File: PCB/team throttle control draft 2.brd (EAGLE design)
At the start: 75.9 x 59.7 mm, 15 parts, among them IC1 ICL7663CPA, IC4 7805T

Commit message: It was missing two connections so this is now fixed and fully operating design
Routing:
- net WH_SP3_D: track 0.00 -> 20.9 mm
- net WH_SP4_D: track 0.00 -> 20.9 mm
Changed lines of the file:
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@@
 <contactref element="WHEEL_SP3" pad="2"/>
 <contactref element="U$3" pad="18-A4/SDA0"/>
-<wire x1="53.34" y1="50.8" x2="53.34" y2="66.04" width="0" layer="19" extent="1-1"/>
+<wire x1="53.34" y1="66.04" x2="52.07" y2="64.77" width="0.3048" layer="16"/>
+<wire x1="52.07" y1="64.77" x2="49.53" y2="64.77" width="0.3048" layer="16"/>
+<wire x1="49.53" y1="64.77" x2="48.26" y2="63.5" width="0.3048" layer="16"/>
+<wire x1="48.26" y1="63.5" x2="48.26" y2="62.23" width="0.3048" layer="16"/>
+<wire x1="53.34" y1="57.15" x2="53.34" y2="50.8" width="0.3048" layer="16"/>
+<wire x1="48.26" y1="62.23" x2="53.34" y2="57.15" width="0.3048" layer="16"/>
 </signal>
 <signal name="WH_SP4_D">
 <contactref element="WHEEL_SP4" pad="2"/>
 <contactref element="U$3" pad="19-A5/SCL0"/>
-<wire x1="50.8" y1="50.8" x2="50.8" y2="66.04" width="0" layer="19" extent="1-1"/>
+<wire x1="45.72" y1="63.5" x2="45.72" y2="59.69" width="0.3048" layer="16"/>
+<wire x1="45.72" y1="59.69" x2="50.8" y2="54.61" width="0.3048" layer="16"/>
+<wire x1="50.8" y1="54.61" x2="50.8" y2="50.8" width="0.3048" layer="16"/>
+<wire x1="50.8" y1="66.04" x2="48.26" y2="66.04" width="0.3048" layer="16"/>
+<wire x1="48.26" y1="66.04" x2="45.72" y2="63.5" width="0.3048" layer="16"/>
 </signal>
 <signal name="ACC_DATA_OUT_1">

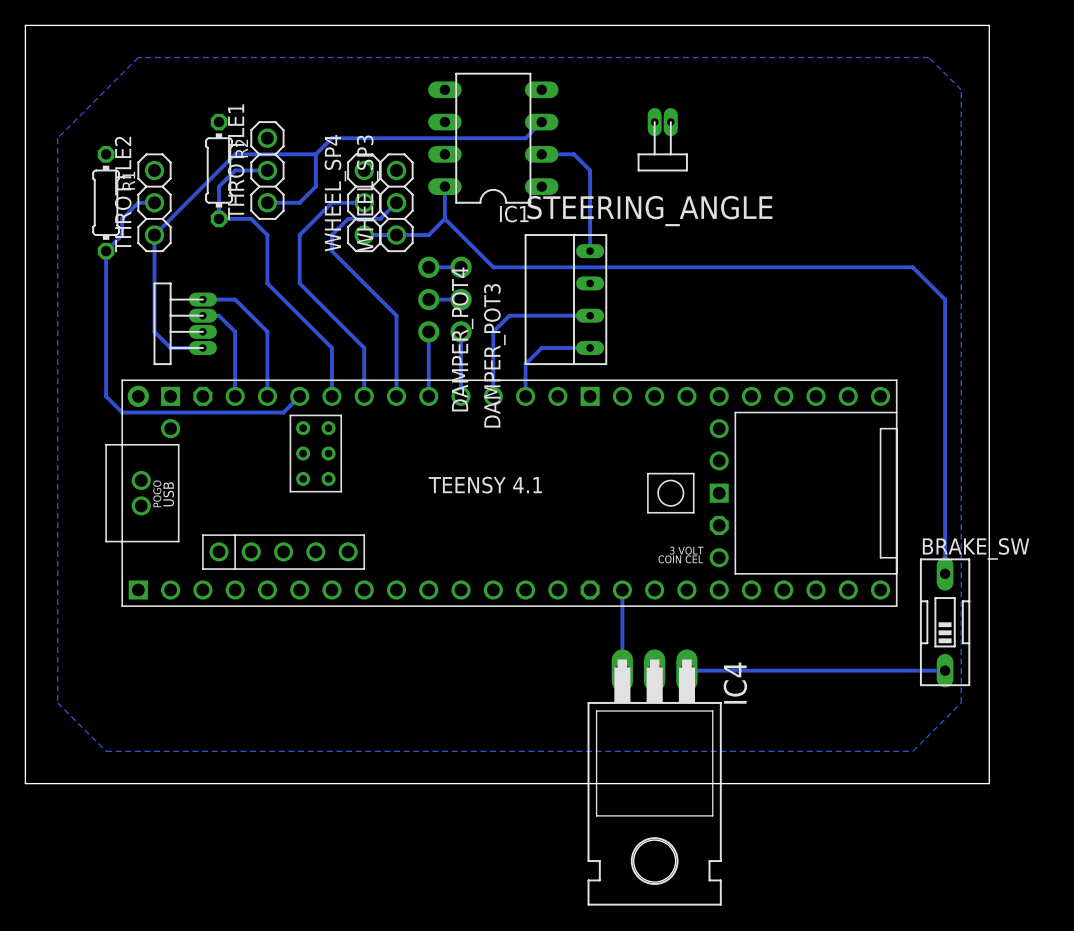
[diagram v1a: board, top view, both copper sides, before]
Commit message: Remove voltage regulator. Add 3-pin header. Connect 3.3V wire
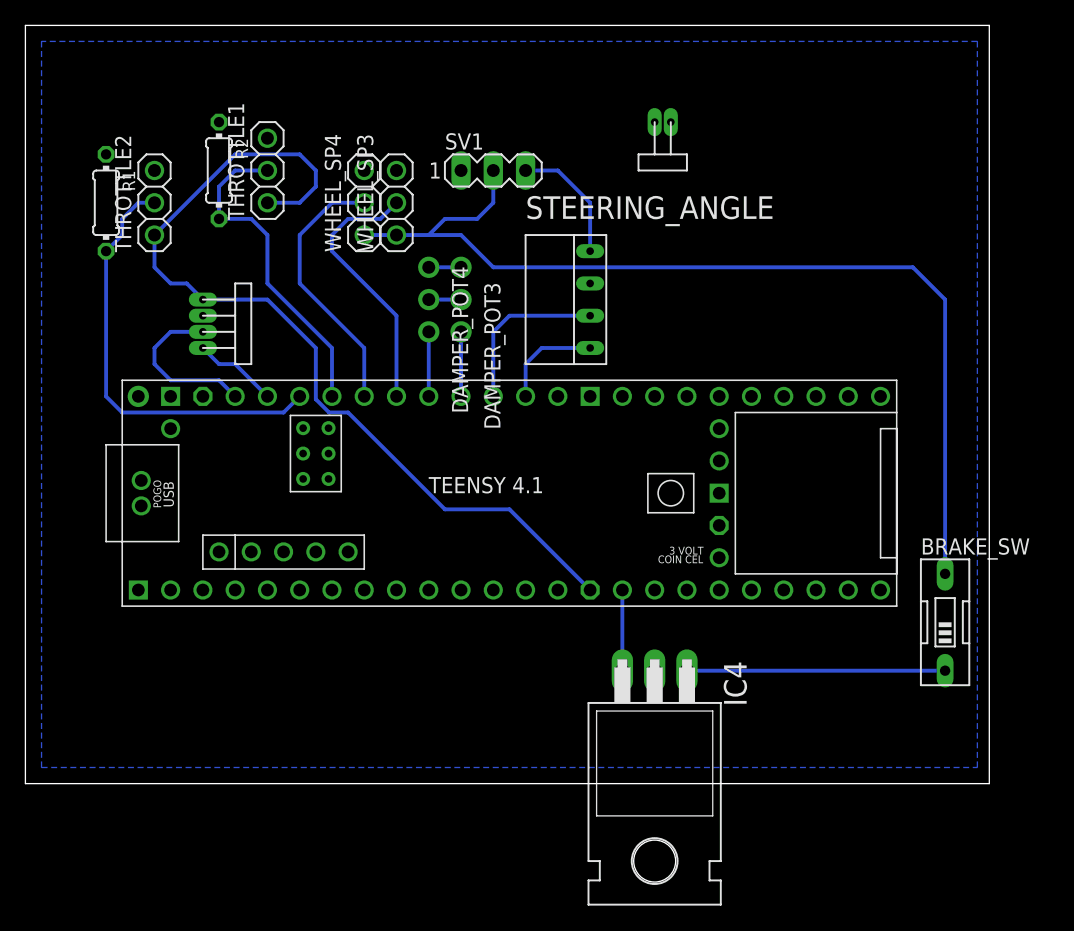
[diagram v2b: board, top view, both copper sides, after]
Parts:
- removed IC1: ICL7663CPA, maxim:DIL08
- added SV1: (no value), con-lstb:MA03-1
- moved U$11 9.25 mm to (36.8, 61.0), turned to 270 degrees
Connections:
- net 12V: now also SV1.2; no longer IC1.8
- net 3.3V: now also U$3.3V3-1; no longer IC1.3
- net 5V: now also SV1.3; no longer IC1.2
- net GND: now also SV1.1; no longer IC1.4
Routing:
- net 3.3V: track 53.0 -> 71.2 mm
- net 12V: track 73.0 -> 78.1 mm
- net CRX_2: track 8.15 -> 13.0 mm
- net CTX_2: track 11.2 -> 6.66 mm
- net 5V: track 10.7 -> 9.94 mm

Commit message: Retry polygon to fix GND signal
didn't work.
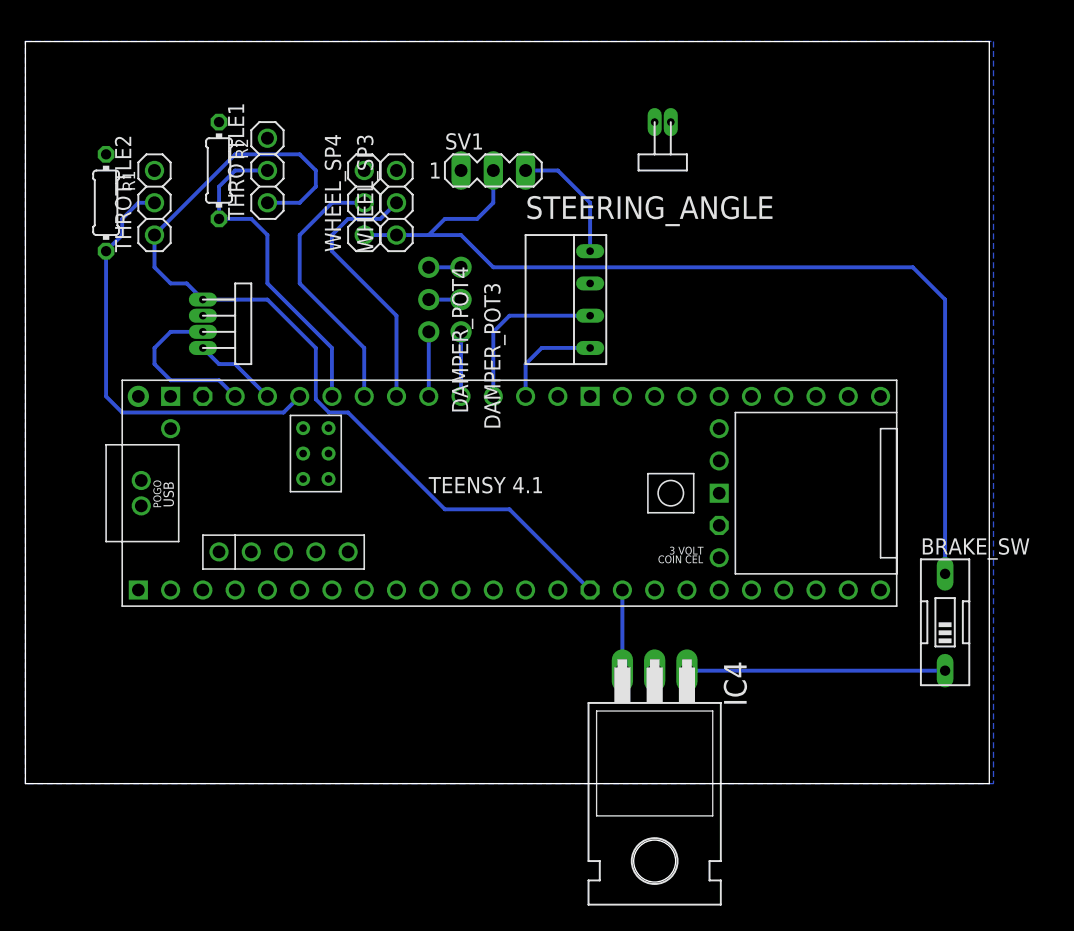
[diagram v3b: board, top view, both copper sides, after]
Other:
- board size 75.9 x 59.7 mm -> 75.9 x 58.4 mm
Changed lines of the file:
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@@
 <plain>
 <wire x1="24.13" y1="20.32" x2="100" y2="20.32" width="0" layer="20"/>
-<wire x1="100" y1="20.32" x2="100" y2="80" width="0" layer="20"/>
-<wire x1="100" y1="80" x2="24.13" y2="80" width="0" layer="20"/>
-<wire x1="24.13" y1="80" x2="24.13" y2="20.32" width="0" layer="20"/>
+<wire x1="100" y1="20.32" x2="100" y2="78.73" width="0" layer="20"/>
+<wire x1="100" y1="78.73" x2="24.13" y2="78.73" width="0" layer="20"/>
+<wire x1="24.13" y1="78.73" x2="24.13" y2="20.32" width="0" layer="20"/>
 </plain>
 <attributes>
@@
 <contactref element="SV1" pad="1"/>
 <polygon width="0.3048" layer="16">
-<vertex x="25.4" y="78.74"/>
-<vertex x="25.4" y="21.59"/>
-<vertex x="99.06" y="21.59"/>
-<vertex x="99.06" y="78.74"/>
+<vertex x="24.13" y="78.74"/>
+<vertex x="100.33" y="78.74"/>
+<vertex x="100.33" y="20.32"/>
+<vertex x="24.13" y="20.32"/>
 </polygon>
 <wire x1="68.58" y1="50.8" x2="68.58" y2="59.69" width="0" layer="19" extent="1-1"/>
